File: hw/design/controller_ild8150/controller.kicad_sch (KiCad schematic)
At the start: 45 parts, among them J1 Conn_ARM_SWD_TagConnect_TC203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, J3 Conn_02x01, U3 ILD8150, U300 MCP2021A-330E/SN, U4 ATSAMC21E18A-MNT

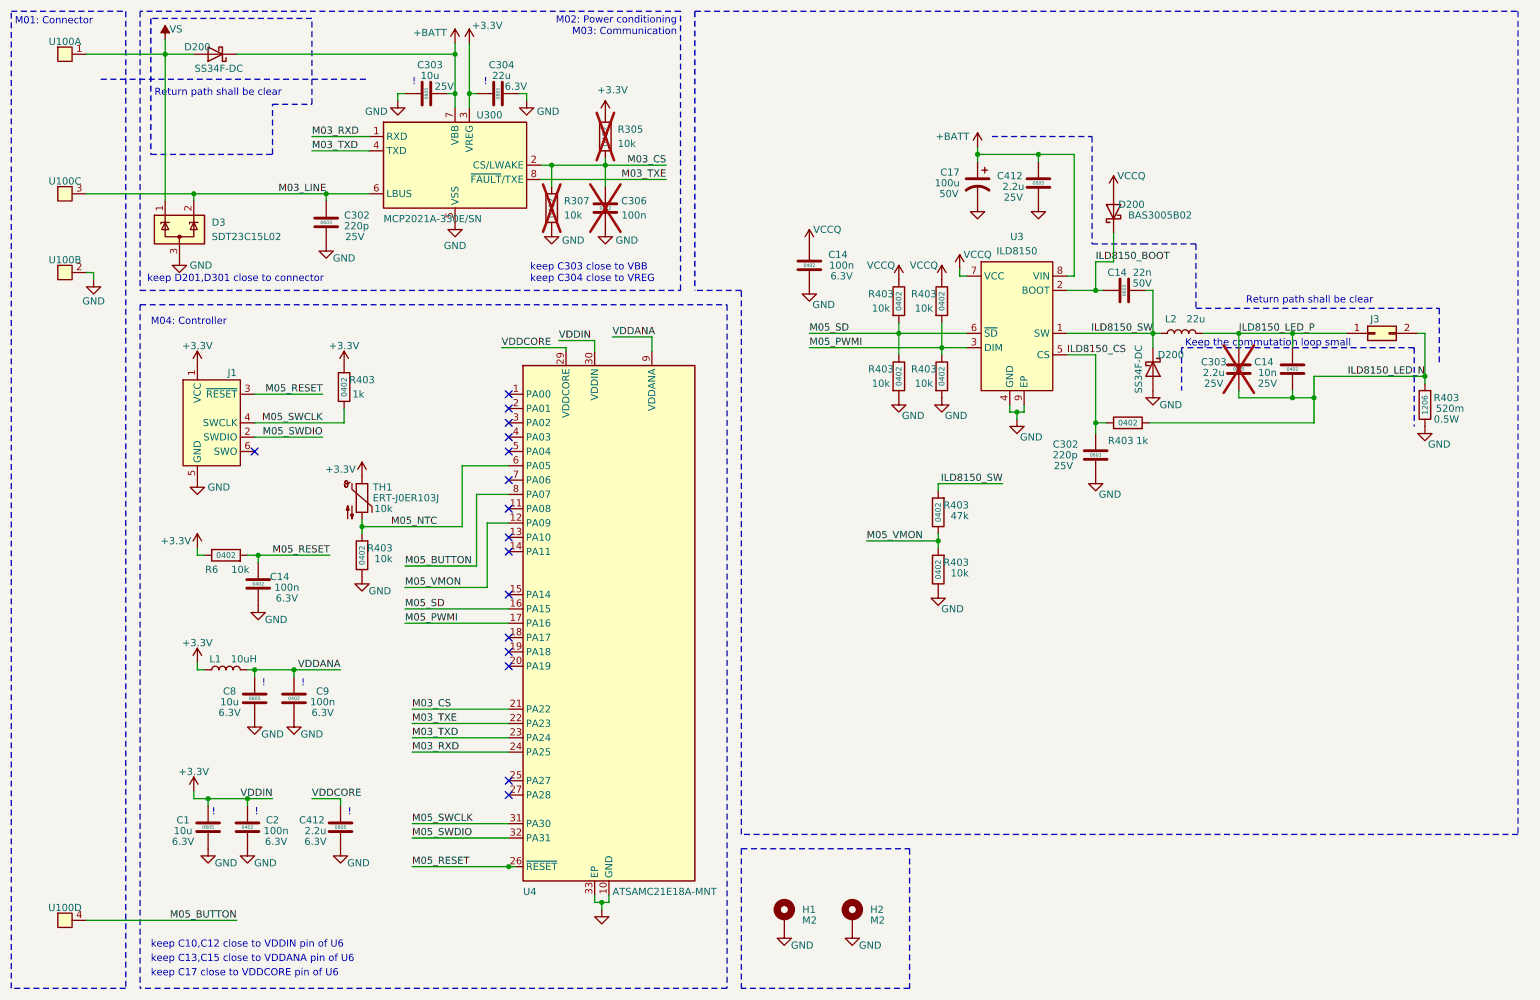
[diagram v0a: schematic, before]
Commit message: Hardware schematic cleanup
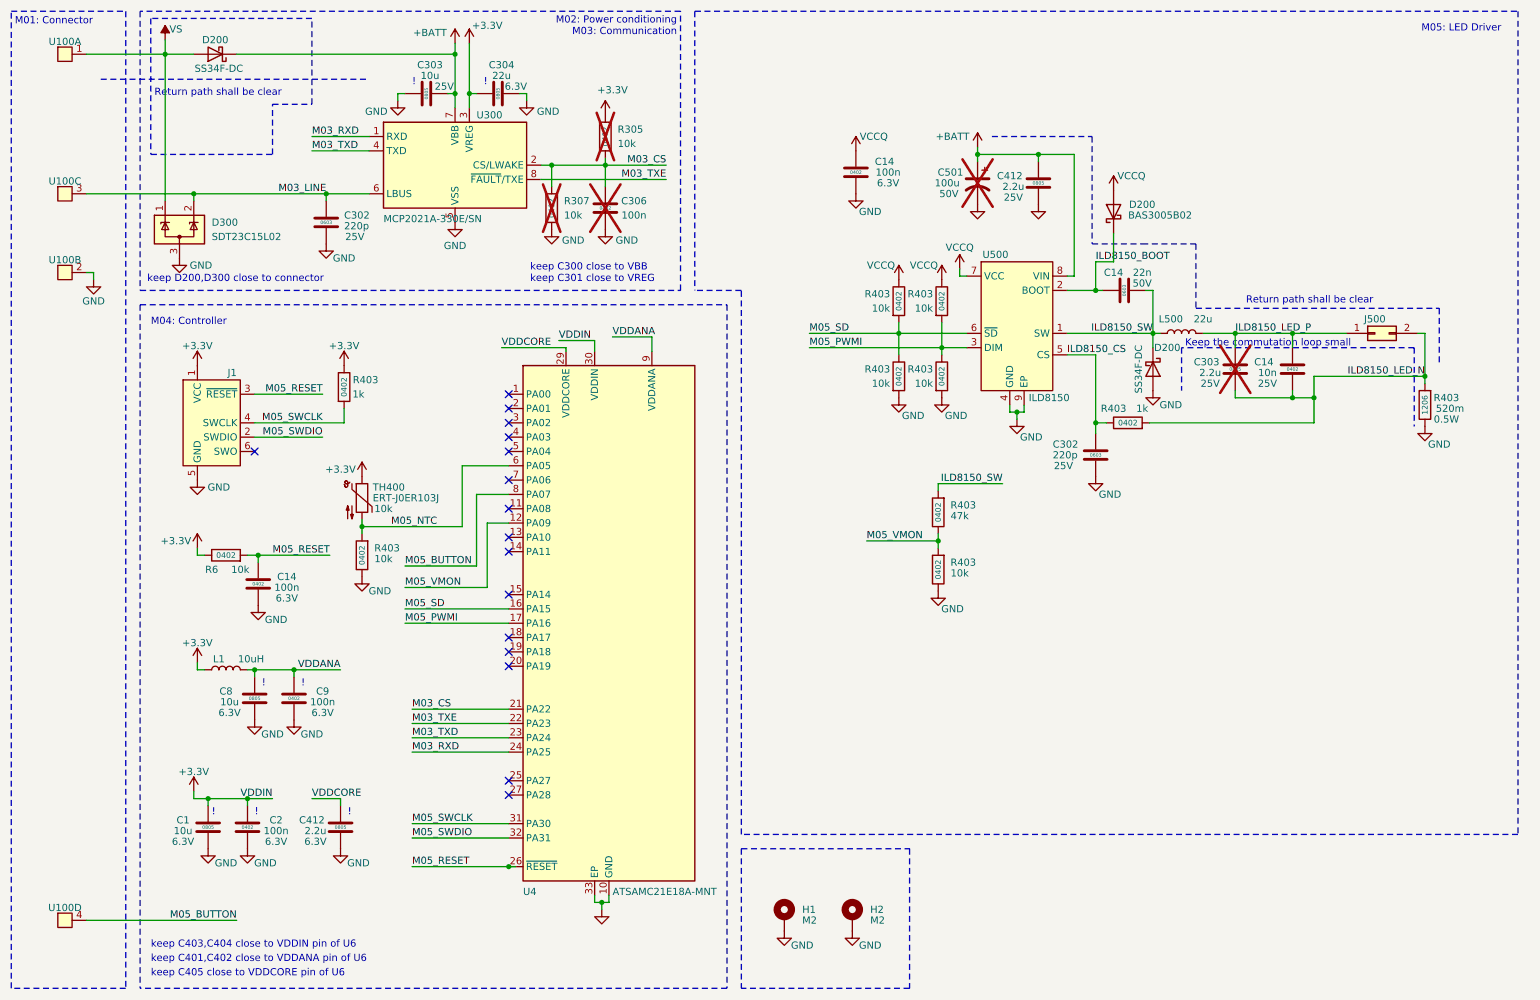
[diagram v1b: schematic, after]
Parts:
- C501: renamed from C17; now not fitted
- renumbered D3 to D300, J3 to J500, L2 to L500, TH1 to TH400, U3 to U500
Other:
- note added: "M05: LED Driver"
- note added: "keep C300 close to VBB keep C301 close to VREG"
- note added: "keep C401,C402 close to VDDANA pin of U6"
- note added: "keep C403,C404 close to VDDIN pin of U6"
- note added: "keep C405 close to VDDCORE pin of U6"
- note added: "keep D200,D300 close to connector"
- note removed: "keep C10,C12 close to VDDIN pin of U6"
- note removed: "keep C13,C15 close to VDDANA pin of U6"
- note removed: "keep C17 close to VDDCORE pin of U6"
- note removed: "keep C303 close to VBB keep C304 close to VREG"
- note removed: "keep D201,D301 close to connector"
- moved on the sheet: C14, C303
